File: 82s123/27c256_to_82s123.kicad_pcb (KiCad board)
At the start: 2 copper layers, 17.8 x 36.5 mm, 2 parts, among them J1 Conn_02x08_Counter_Clockwise, U1 27C256

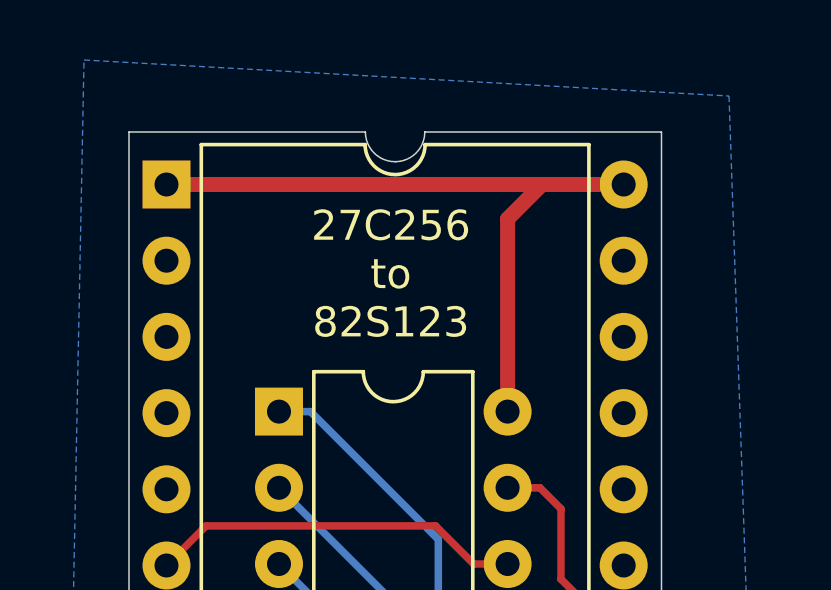
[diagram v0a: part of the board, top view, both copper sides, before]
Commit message: Changed the silkscreen on the PCB to be more specific
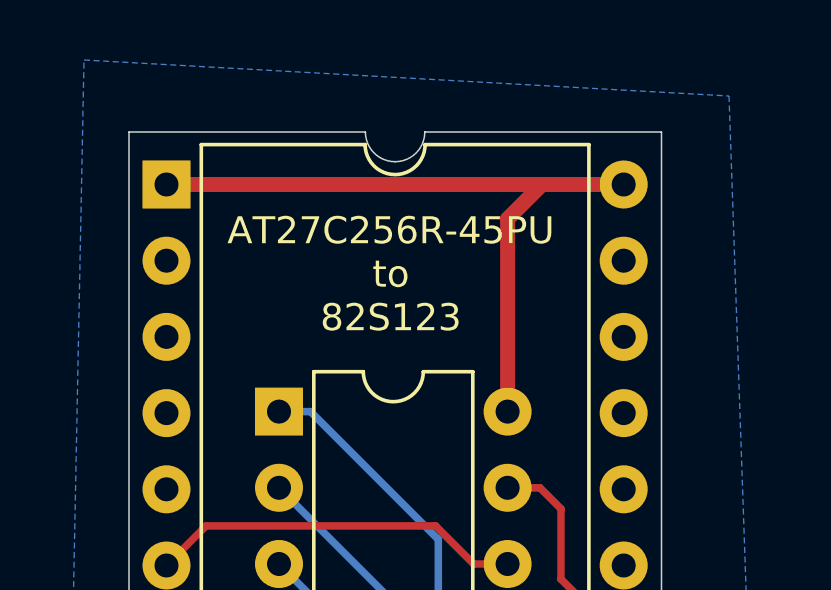
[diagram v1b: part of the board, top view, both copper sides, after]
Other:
- board text added: "AT27C256R-45PU to 82S123"
- board text removed: "27C256 to 82S123"
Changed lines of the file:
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@@
     )
   )
-  (gr_text "27C256\nto\n82S123" (at 164.73 90.24) (layer F.SilkS)
-    (effects (font (size 1 1) (thickness 0.15)))
+  (gr_text "AT27C256R-45PU\nto\n82S123" (at 164.73 90.24) (layer F.SilkS)
+    (effects (font (size 0.9 0.9) (thickness 0.15)))
   )
   (gr_line (start 173.75 85.5) (end 165.86 85.5) (layer Edge.Cuts) (width 0.05))
